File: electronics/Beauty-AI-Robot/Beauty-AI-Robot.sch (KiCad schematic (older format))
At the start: 7 parts, among them M1 Stepper_Motor_bipolar, M2 Motor_Servo

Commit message: update schematic
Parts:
- added R1: 470, symbol Device:R_US
- A2: symbol BigEasyDriver:BigEasyDriver -> Beauty-AI-Robot-rescue:BigEasyDriver-BigEasyDriver
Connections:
- net at A1.26 (D11): now also R1.1; no longer A3.~ (GND)
- new net: A3.~ (GND), R1.2
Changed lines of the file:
@@
 $EndComp
 $Comp
-L BigEasyDriver:BigEasyDriver A2
+L Beauty-AI-Robot-rescue:BigEasyDriver-BigEasyDriver A2
 U 1 1 613E90F8
 P 3900 3300
@@
 	3600 4950 3600 5550
 Wire Wire Line
-	3600 5550 5150 5550
-Wire Wire Line
-	5150 5550 5150 4200
-Wire Wire Line
-	5150 4200 5600 4200
+	3600 5550 5000 5550
 Wire Wire Line
 	3600 4850 3450 4850
@@
 Wire Wire Line
 	2450 4500 2450 4550
+$Comp
+L Device:R_US R1
+U 1 1 613D9CFF
+P 5000 5400
+F 0 "R1" H 5068 5446 50  0000 L CNN
+F 1 "470" H 5068 5355 50  0000 L CNN
+F 2 "" V 5040 5390 50  0001 C CNN
+F 3 "~" H 5000 5400 50  0001 C CNN
+	1    5000 5400
+	1    0    0    -1
+$EndComp
+Wire Wire Line
+	5000 5250 5000 4200
+Wire Wire Line
+	5000 4200 5600 4200
 $EndSCHEMATC

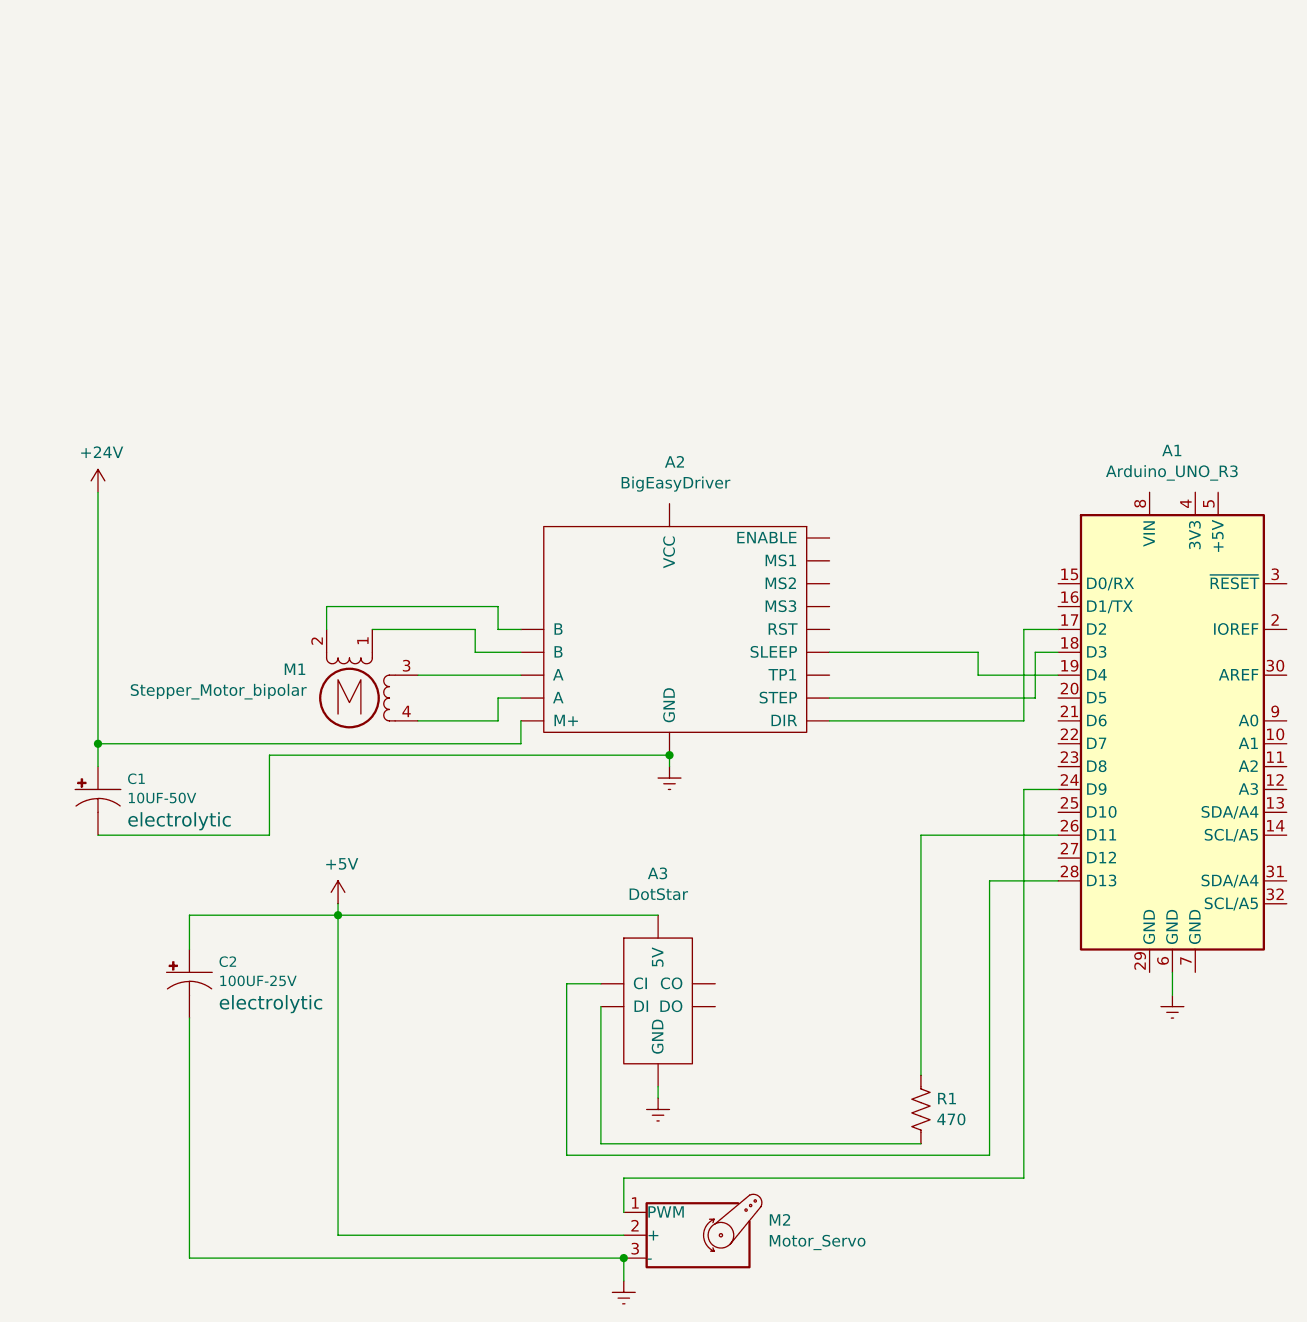
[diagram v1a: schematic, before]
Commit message: schematic change (add driver for bioremediation syringe pump)
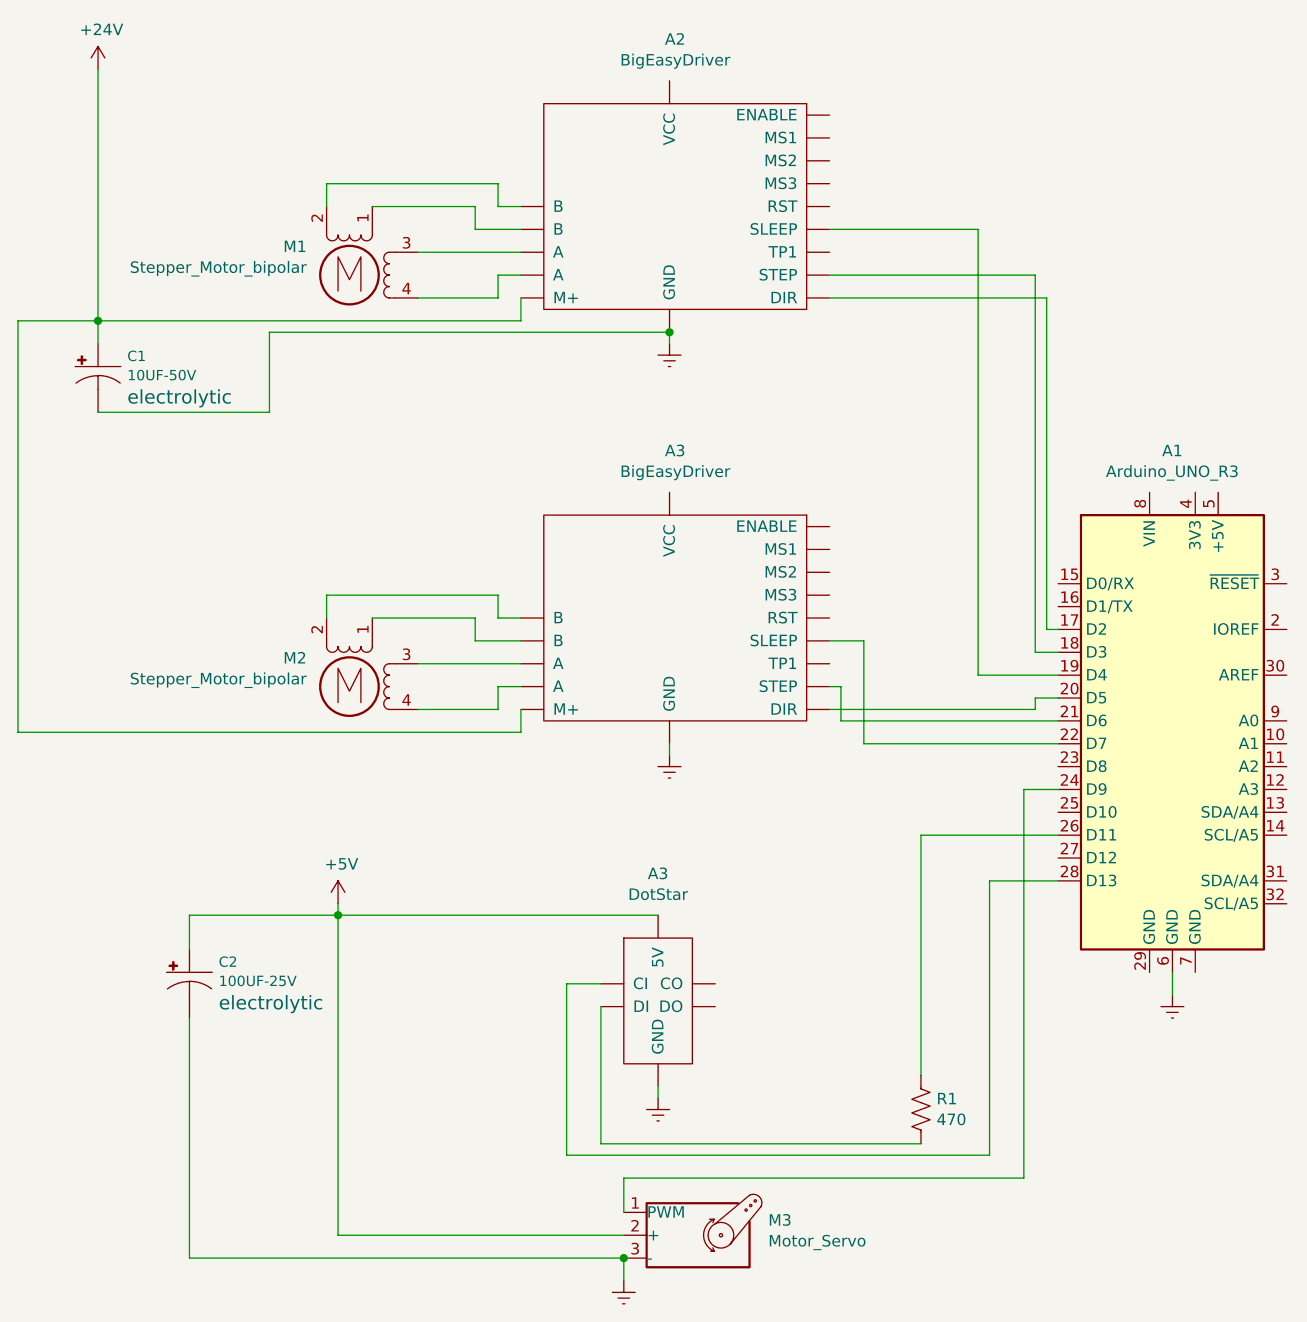
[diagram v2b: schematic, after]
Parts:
- added A3: BigEasyDriver, symbol Beauty-AI-Robot-rescue:BigEasyDriver-BigEasyDriver
- added M2: Stepper_Motor_bipolar, symbol Motor:Stepper_Motor_bipolar
- renumbered M2 to M3
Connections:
- net +24V: now also A3.~ (VCC)
- net Earth: now also A3.~ (VCC)
- net at A1.20 (D5): now also A3.~ (VCC)
- net at A1.21 (D6): now also A3.~ (VCC)
- net at A1.22 (D7): now also A3.~ (VCC)
- new net: A3.~ (VCC), M2.1
- new net: A3.~ (VCC), M2.2 (-)
- new net: A3.~ (VCC), M2.3
- new net: A3.~ (VCC), M2.4
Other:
- moved on the sheet: A2, C1, M1
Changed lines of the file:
@@
-$EndComp
-$Comp
-L Beauty-AI-Robot-rescue:BigEasyDriver-BigEasyDriver A2
-U 1 1 613E90F8
-P 3900 3300
-F 0 "A2" H 3875 4031 50  0000 C CNN
-F 1 "BigEasyDriver" H 3875 3940 50  0000 C CNN
-F 2 "" H 3900 3450 50  0001 C CNN
-F 3 "http://www.schmalzhaus.com/BigEasyDriver/BigEasyDriver_UserManal.pdf" H 3900 3450 50  0001 C CNN
-	1    3900 3300
-	-1   0    0    -1
 $EndComp
 $Comp
@@
 $EndComp
 Wire Wire Line
-	1400 3800 3250 3800
-Wire Wire Line
-	3250 3800 3250 3700
-Wire Wire Line
-	3150 3700 3150 3600
-Wire Wire Line
-	3150 3600 3250 3600
-Wire Wire Line
-	2800 3700 3150 3700
-$Comp
-L Motor:Stepper_Motor_bipolar M1
-U 1 1 613F4373
-P 2500 3600
-F 0 "M1" H 2687 3724 50  0000 L CNN
-F 1 "Stepper_Motor_bipolar" H 2687 3633 50  0000 L CNN
-F 2 "" H 2510 3590 50  0001 C CNN
-F 3 "http://www.infineon.com/dgdl/Application-Note-TLE8110EE_driving_UniPolarStepperMotor_V1.1.pdf?fileId=db3a30431be39b97011be5d0aa0a00b0" H 2510 3590 50  0001 C CNN
-	1    2500 3600
-	-1   0    0    -1
-$EndComp
-Wire Wire Line
-	2800 3500 3250 3500
-Wire Wire Line
-	2600 3300 3050 3300
-Wire Wire Line
-	3050 3300 3050 3400
-Wire Wire Line
-	3050 3400 3250 3400
-Wire Wire Line
-	2400 3300 2400 3200
-Wire Wire Line
-	2400 3200 3150 3200
-Wire Wire Line
-	3150 3200 3150 3300
-Wire Wire Line
-	3150 3300 3250 3300
-Wire Wire Line
 	2450 4550 3850 4550
 Connection ~ 2450 4550
@@
 	2450 5950 3700 5950
 $Comp
-L Motor:Motor_Servo M2
+L Motor:Motor_Servo M3
 U 1 1 613F220D
 P 4000 5950
-F 0 "M2" H 4332 6015 50  0000 L CNN
+F 0 "M3" H 4332 6015 50  0000 L CNN
 F 1 "Motor_Servo" H 4332 5924 50  0000 L CNN
 F 2 "" H 4000 5760 50  0001 C CNN
@@
 	1    0    0    -1
 $EndComp
-$Comp
-L power:Earth #PWR?
-U 1 1 6140409B
-P 3900 3900
-F 0 "#PWR?" H 3900 3650 50  0001 C CNN
-F 1 "Earth" H 3900 3750 50  0001 C CNN
-F 2 "" H 3900 3900 50  0001 C CNN
-F 3 "~" H 3900 3900 50  0001 C CNN
-	1    3900 3900
-	1    0    0    -1
-$EndComp
-Wire Wire Line
-	3900 3850 3900 3900
 Wire Wire Line
 	2450 4550 2450 5950
@@
 Wire Wire Line
 	6100 4800 6100 4900
-$Comp
-L SparkFun-Capacitors:10UF-POLAR-RADIAL-2.5MM-25V-20% C1
-U 1 1 6140A070
-P 1400 4000
-F 0 "C1" H 1528 4045 45  0000 L CNN
-F 1 "10UF-50V" H 1528 3961 45  0000 L CNN
-F 2 "CPOL-RADIAL-2.5MM-5MM" H 1400 4250 20  0001 C CNN
-F 3 "" H 1400 4000 50  0001 C CNN
-F 4 "electrolytic" H 1528 3866 60  0000 L CNN "Field4"
-	1    1400 4000
-	1    0    0    -1
-$EndComp
-Wire Wire Line
-	1400 3900 1400 3800
-Connection ~ 1400 3800
-Wire Wire Line
-	1400 4200 2150 4200
-Wire Wire Line
-	2150 4200 2150 3850
-Wire Wire Line
-	2150 3850 3900 3850
-Connection ~ 3900 3850
 $Comp
 L SparkFun-Capacitors:100UF-POLAR-RADIAL-2.5MM-25V-20% C2
@@
 Connection ~ 3700 6050
 Wire Wire Line
-	4600 3700 5450 3700
-Wire Wire Line
-	5450 3700 5450 3300
-Wire Wire Line
-	5450 3300 5600 3300
-Wire Wire Line
-	4600 3600 5500 3600
-Wire Wire Line
-	5500 3600 5500 3400
-Wire Wire Line
-	5500 3400 5600 3400
-Wire Wire Line
 	3700 5850 3700 5700
 Wire Wire Line
@@
 Wire Wire Line
 	5300 4400 5600 4400
-Wire Wire Line
-	4600 3400 5250 3400
-Wire Wire Line
-	5250 3400 5250 3500
-Wire Wire Line
-	5250 3500 5600 3500
-$Comp
-L power:+24V #PWR?
-U 1 1 613F687D
-P 1400 2700
-F 0 "#PWR?" H 1400 2550 50  0001 C CNN
-F 1 "+24V" H 1415 2873 50  0000 C CNN
-F 2 "" H 1400 2700 50  0001 C CNN
-F 3 "" H 1400 2700 50  0001 C CNN
-	1    1400 2700
-	1    0    0    -1
-$EndComp
-Wire Wire Line
-	1400 2700 1400 3800
 $Comp
 L power:+5V #PWR?
@@
 Wire Wire Line
 	5000 4200 5600 4200
+$Comp
+L Beauty-AI-Robot-rescue:BigEasyDriver-BigEasyDriver A2
+U 1 1 613E90F8
+P 3900 1450
+F 0 "A2" H 3875 2181 50  0000 C CNN
+F 1 "BigEasyDriver" H 3875 2090 50  0000 C CNN
+F 2 "" H 3900 1600 50  0001 C CNN
+F 3 "http://www.schmalzhaus.com/BigEasyDriver/BigEasyDriver_UserManal.pdf" H 3900 1600 50  0001 C CNN
+	1    3900 1450
+	-1   0    0    -1
+$EndComp
+Wire Wire Line
+	1400 1950 3250 1950
+Wire Wire Line
+	3250 1950 3250 1850
+Wire Wire Line
+	3150 1850 3150 1750
+Wire Wire Line
+	3150 1750 3250 1750
+Wire Wire Line
+	2800 1850 3150 1850
+$Comp
+L Motor:Stepper_Motor_bipolar M1
+U 1 1 613F4373
+P 2500 1750
+F 0 "M1" H 2687 1874 50  0000 L CNN
+F 1 "Stepper_Motor_bipolar" H 2687 1783 50  0000 L CNN
+F 2 "" H 2510 1740 50  0001 C CNN
+F 3 "http://www.infineon.com/dgdl/Application-Note-TLE8110EE_driving_UniPolarStepperMotor_V1.1.pdf?fileId=db3a30431be39b97011be5d0aa0a00b0" H 2510 1740 50  0001 C CNN
+	1    2500 1750
+	-1   0    0    -1
+$EndComp
+Wire Wire Line
+	2800 1650 3250 1650
+Wire Wire Line
+	2600 1450 3050 1450
+Wire Wire Line
+	3050 1450 3050 1550
+Wire Wire Line
+	3050 1550 3250 1550
+Wire Wire Line
+	2400 1450 2400 1350
+Wire Wire Line
+	2400 1350 3150 1350
+Wire Wire Line
+	3150 1350 3150 1450
+Wire Wire Line
+	3150 1450 3250 1450
+$Comp
+L power:Earth #PWR?
+U 1 1 6140409B
+P 3900 2050
+F 0 "#PWR?" H 3900 1800 50  0001 C CNN
+F 1 "Earth" H 3900 1900 50  0001 C CNN
+F 2 "" H 3900 2050 50  0001 C CNN
+F 3 "~" H 3900 2050 50  0001 C CNN
+	1    3900 2050
+	1    0    0    -1
+$EndComp
+Wire Wire Line
+	3900 2000 3900 2050
+$Comp
+L SparkFun-Capacitors:10UF-POLAR-RADIAL-2.5MM-25V-20% C1
+U 1 1 6140A070
+P 1400 2150
+F 0 "C1" H 1528 2195 45  0000 L CNN
+F 1 "10UF-50V" H 1528 2111 45  0000 L CNN
+F 2 "CPOL-RADIAL-2.5MM-5MM" H 1400 2400 20  0001 C CNN
+F 3 "" H 1400 2150 50  0001 C CNN
+F 4 "electrolytic" H 1528 2016 60  0000 L CNN "Field4"
+	1    1400 2150
+	1    0    0    -1
+$EndComp
+Wire Wire Line
+	1400 2050 1400 1950
+Connection ~ 1400 1950
+Wire Wire Line
+	2150 2350 2150 2000
+Wire Wire Line
+	2150 2000 3900 2000
+Connection ~ 3900 2000
+Wire Wire Line
+	4600 1750 5500 1750
+Wire Wire Line
+	4600 1550 5250 1550
+$Comp
+L power:+24V #PWR?
+U 1 1 613F687D
+P 1400 850
+F 0 "#PWR?" H 1400 700 50  0001 C CNN
+F 1 "+24V" H 1415 1023 50  0000 C CNN
+F 2 "" H 1400 850 50  0001 C CNN
+F 3 "" H 1400 850 50  0001 C CNN
+	1    1400 850
+	1    0    0    -1
+$EndComp
+Wire Wire Line
+	1400 850  1400 1950
+$Comp
+L Beauty-AI-Robot-rescue:BigEasyDriver-BigEasyDriver A3
+U 1 1 61498DC1
+P 3900 3250
+F 0 "A3" H 3875 3981 50  0000 C CNN
+F 1 "BigEasyDriver" H 3875 3890 50  0000 C CNN
+F 2 "" H 3900 3400 50  0001 C CNN
+F 3 "http://www.schmalzhaus.com/BigEasyDriver/BigEasyDriver_UserManal.pdf" H 3900 3400 50  0001 C CNN
+	1    3900 3250
+	-1   0    0    -1
+$EndComp
+Wire Wire Line
+	3150 3650 3150 3550
+Wire Wire Line
+	3150 3550 3250 3550
+Wire Wire Line
+	2800 3650 3150 3650
+$Comp
+L Motor:Stepper_Motor_bipolar M2
+U 1 1 61498DCC
+P 2500 3550
+F 0 "M2" H 2687 3674 50  0000 L CNN
+F 1 "Stepper_Motor_bipolar" H 2687 3583 50  0000 L CNN
+F 2 "" H 2510 3540 50  0001 C CNN
+F 3 "http://www.infineon.com/dgdl/Application-Note-TLE8110EE_driving_UniPolarStepperMotor_V1.1.pdf?fileId=db3a30431be39b97011be5d0aa0a00b0" H 2510 3540 50  0001 C CNN
+	1    2500 3550
+	-1   0    0    -1
+$EndComp
+Wire Wire Line
+	2800 3450 3250 3450
+Wire Wire Line
+	2600 3250 3050 3250
+Wire Wire Line
+	3050 3250 3050 3350
+Wire Wire Line
+	3050 3350 3250 3350
+Wire Wire Line
+	2400 3250 2400 3150
+Wire Wire Line
+	2400 3150 3150 3150
+Wire Wire Line
+	3150 3150 3150 3250
+Wire Wire Line
+	3150 3250 3250 3250
+$Comp
+L power:Earth #PWR?
+U 1 1 61498DDA
+P 3900 3850
+F 0 "#PWR?" H 3900 3600 50  0001 C CNN
+F 1 "Earth" H 3900 3700 50  0001 C CNN
+F 2 "" H 3900 3850 50  0001 C CNN
+F 3 "~" H 3900 3850 50  0001 C CNN
+	1    3900 3850
+	1    0    0    -1
+$EndComp
+Wire Wire Line
+	3900 3800 3900 3850
+Wire Wire Line
+	1400 2350 2150 2350
+Wire Wire Line
+	3250 3650 3250 3750
+Wire Wire Line
+	3250 3750 1050 3750
+Wire Wire Line
+	1050 3750 1050 1950
+Wire Wire Line
+	1050 1950 1400 1950
+Wire Wire Line
+	4600 1850 5550 1850
+Wire Wire Line
+	5550 1850 5550 3300
+Wire Wire Line
+	5550 3300 5600 3300
+Wire Wire Line
+	5500 1750 5500 3400
+Wire Wire Line
+	5500 3400 5600 3400
+Wire Wire Line
+	5250 3500 5600 3500
+Wire Wire Line
+	5250 1550 5250 3500
+Wire Wire Line
+	5500 3650 5500 3600
+Wire Wire Line
+	5500 3600 5600 3600
+Wire Wire Line
+	4600 3650 5500 3650
+Wire Wire Line
+	4600 3550 4650 3550
+Wire Wire Line
+	4650 3550 4650 3700
+Wire Wire Line
+	4650 3700 5600 3700
+Wire Wire Line
+	4600 3350 4750 3350
+Wire Wire Line
+	4750 3350 4750 3800
+Wire Wire Line
+	4750 3800 5600 3800
 $EndSCHEMATC
